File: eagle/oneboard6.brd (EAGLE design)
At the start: 43.1 x 58.5 mm, 5 parts

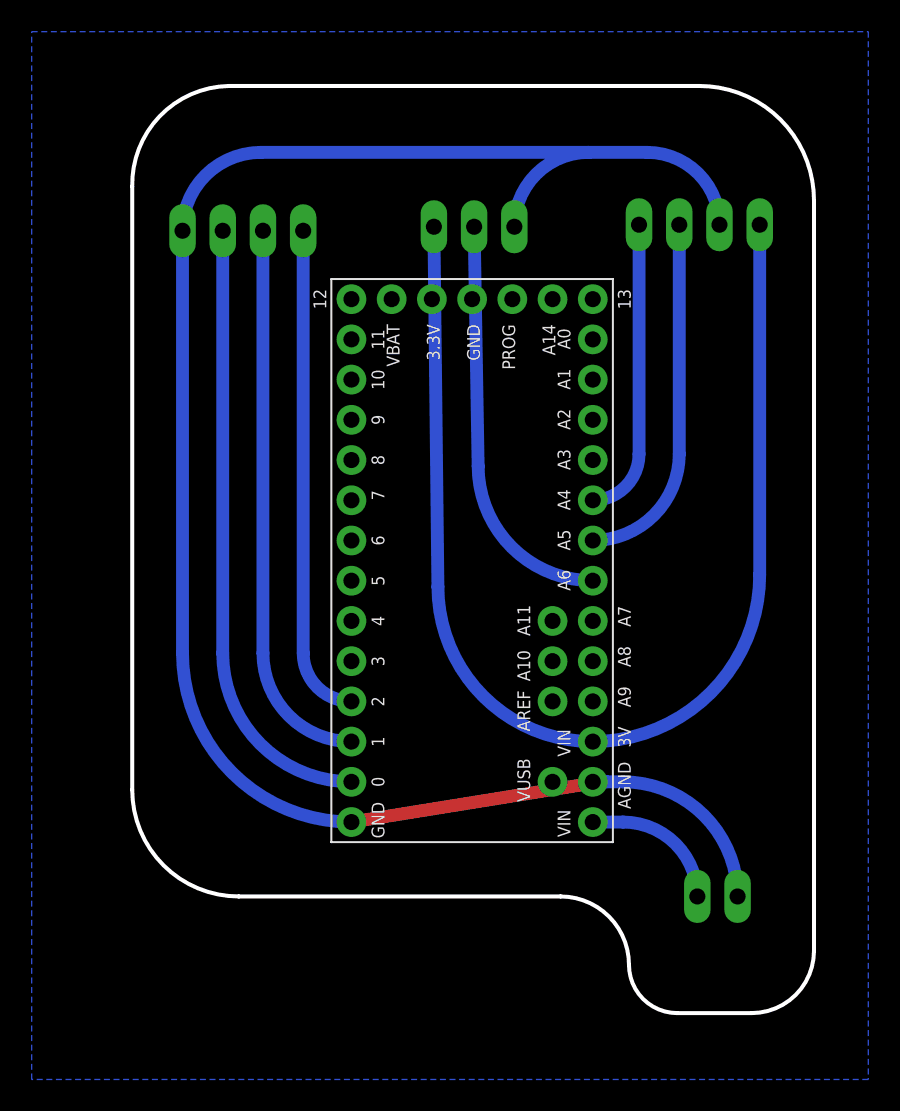
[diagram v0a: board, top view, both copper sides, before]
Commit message: updated eagle board and arduino code
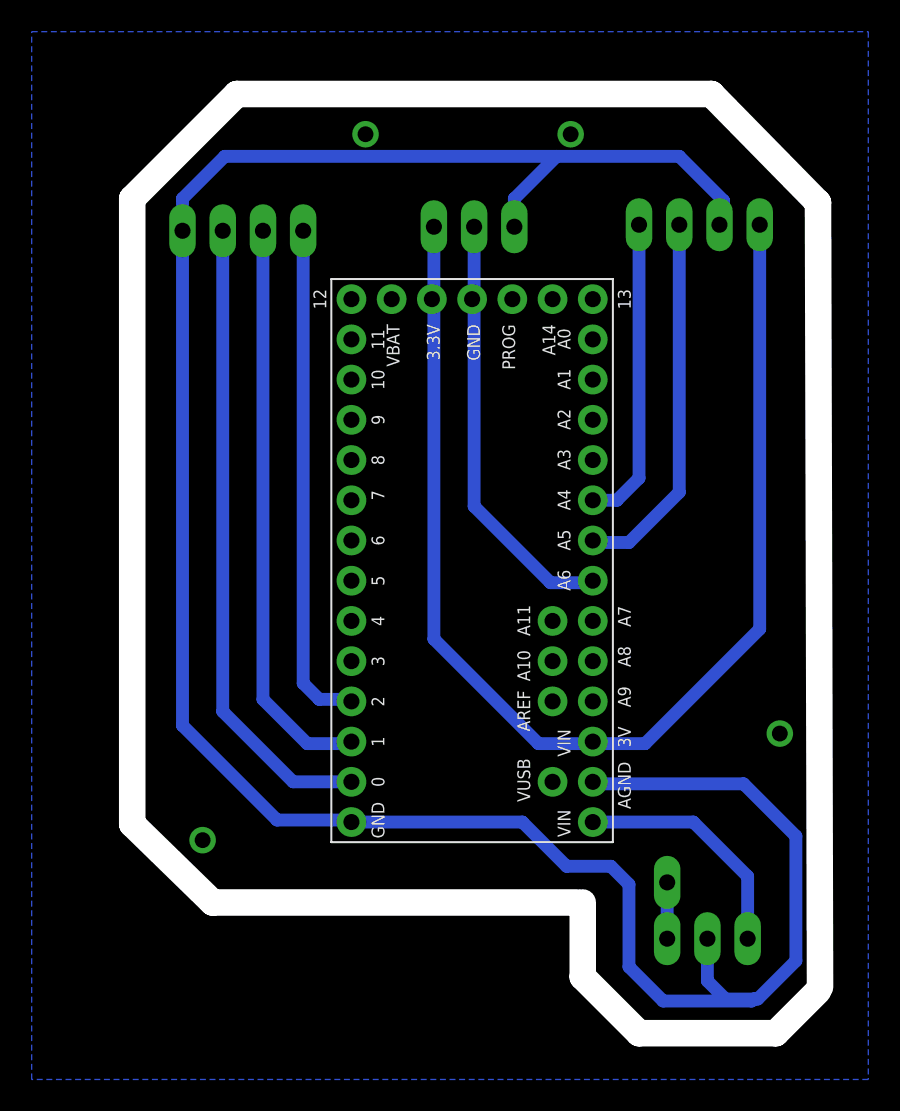
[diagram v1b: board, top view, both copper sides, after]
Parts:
- added U$1: HEADER-3, homemade-hardware:HEADER-3
- U$3: value HEADER-2 -> HEADER-1; device homemade-hardware:HEADER-2 -> homemade-hardware:HEADER-1
- moved U$3 2.10 mm to (40.3, 22.2), turned to 90 degrees
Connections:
- new net N$6: U$1.3, U$3.1
- net GND: now also U$1.2; no longer U$3.2
- net VIN: now also U$1.1; no longer U$3.1
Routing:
- net GND: track 115.7 -> 155.7 mm
- net VIN: track 8.55 -> 15.1 mm
- net VCC: track 73.6 -> 78.0 mm
- net N$6: track 0.00 -> 3.56 mm
- net N$2: track 38.2 -> 40.3 mm
- net NEO: track 25.4 -> 27.2 mm
- net N$1: track 34.6 -> 36.4 mm
- net SCL: track 22.2 -> 23.7 mm
- net N$4: track 31.0 -> 32.1 mm
- net SDA: track 18.6 -> 19.5 mm
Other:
- board size 43.1 x 58.5 mm -> 43.4 x 59.3 mm
